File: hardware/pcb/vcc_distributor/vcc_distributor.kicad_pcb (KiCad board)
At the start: 2 copper layers, 40 x 25.5 mm, 12 parts, among them J1 Screw_Terminal_01x02, J2 Conn_01x02, J3 Conn_01x02, J4 Conn_01x02, J5 Conn_01x02, J6 Conn_01x02, J7 Conn_01x02, J8 Conn_01x02

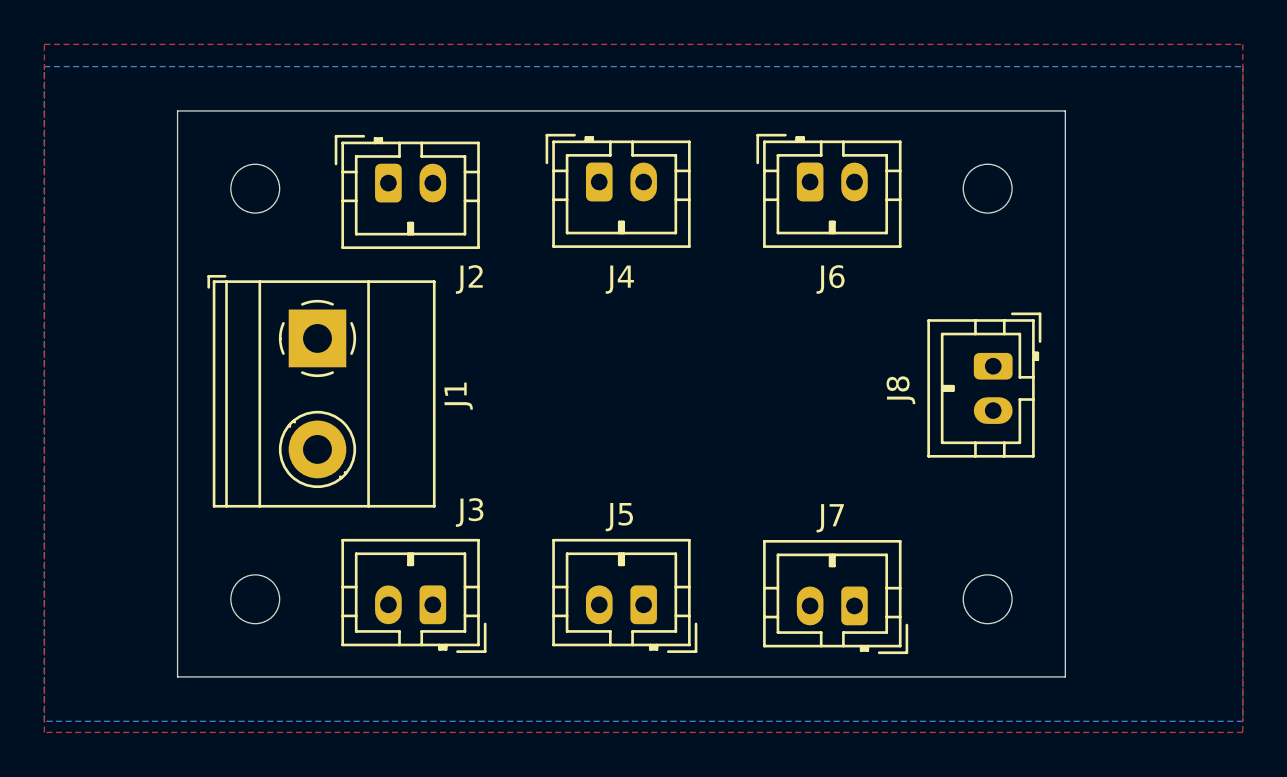
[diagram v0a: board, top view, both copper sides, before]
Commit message: REWORK pcb layout, ADD BOM
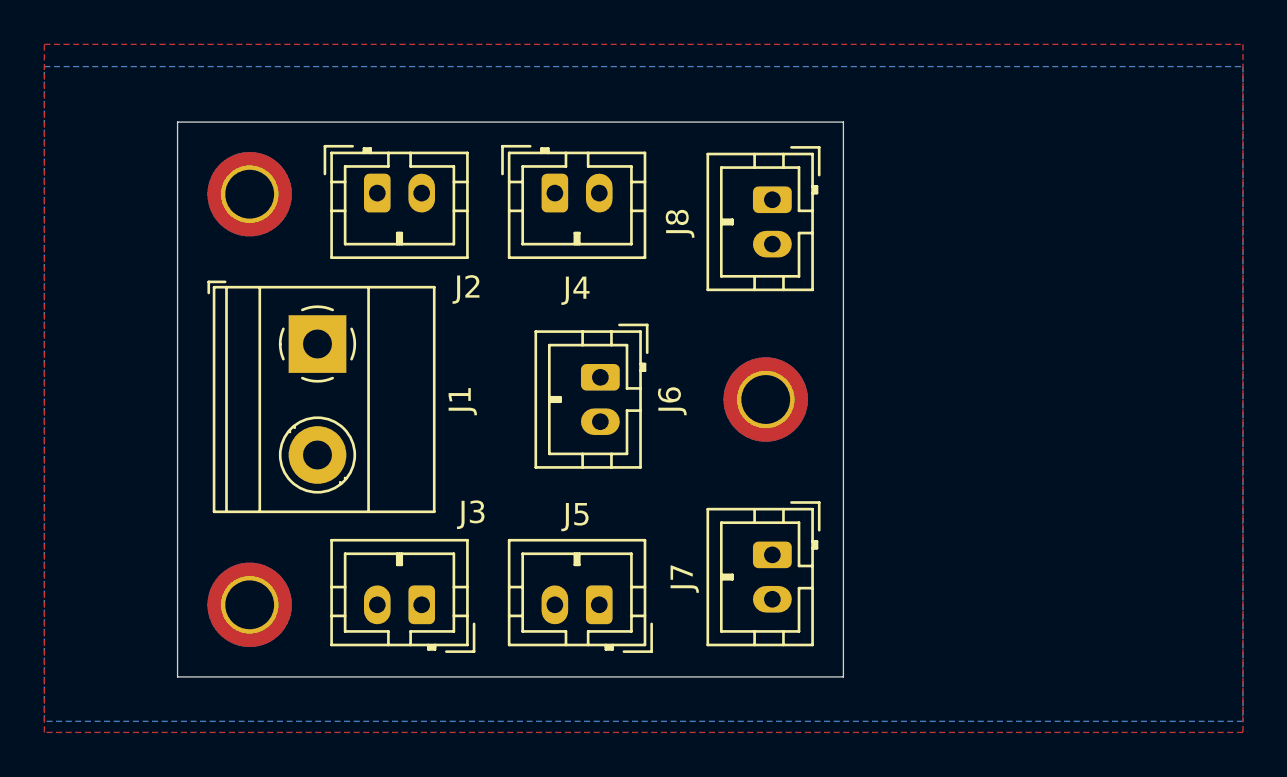
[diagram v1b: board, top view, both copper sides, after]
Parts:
- removed the REF** at (135.5, 49.5)
- REF** (x3): value MountingHole_2.2mm_M2 -> MountingHole_2.2mm_M2_DIN965_Pad_TopBottom; footprint MountingHole:MountingHole_2.2mm_M2 -> MountingHole:MountingHole_2.2mm_M2_DIN965_Pad_TopBottom
- moved REF** 13.5 mm to (125.5, 59.0)
- moved J6 12.9 mm to (118.0, 58.0), turned to -90 degrees
- moved J8 12.5 mm to (125.8, 50.0)
- moved J7 4.36 mm to (125.8, 66.0), turned to -90 degrees
- moved J4 2.06 mm to (116.0, 49.7)
- moved J5 2.00 mm to (118.0, 68.2)
- moved J2 0.67 mm to (108.0, 49.7)
- moved J3 0.50 mm to (110.0, 68.2)
- moved REF** 0.35 mm to (102.2, 68.2)
- moved REF** 0.35 mm to (102.2, 49.8)
- moved J1 0.25 mm to (105.3, 56.5)
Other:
- board size 40 x 25.5 mm -> 30 x 25 mm

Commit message: update gerber files
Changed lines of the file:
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@@
       (outputformat 1)
       (mirror false)
-      (drillshape 1)
+      (drillshape 0)
       (scaleselection 1)
-      (outputdirectory "")
+      (outputdirectory "exports/")
     )
   )
@@
     (fp_line (start -1.95 2.8) (end 3.95 2.8) (layer "F.Fab") (width 0.1))
     (fp_line (start -2.36 -2.11) (end -2.36 -0.86) (layer "F.Fab") (width 0.1))
-    (pad "1" thru_hole roundrect locked (at 0 0 180) (size 1.2 1.75) (drill 0.75) (layers *.Cu *.Mask) (roundrect_rratio 0.208333)
+    (pad "1" thru_hole roundrect locked (at 0 0 180) (size 1.2 1.75) (drill 0.75) (layers *.Cu *.Mask) (roundrect_rratio 0.2083333333)
       (net 1 "GND") (pinfunction "Pin_1") (pintype "passive"))
     (pad "2" thru_hole oval locked (at 2 0 180) (size 1.2 1.75) (drill 0.75) (layers *.Cu *.Mask)
@@
     (fp_line (start -2.36 -2.11) (end -2.36 -0.86) (layer "F.Fab") (width 0.1))
     (fp_line (start -1.11 -2.11) (end -2.36 -2.11) (layer "F.Fab") (width 0.1))
-    (pad "1" thru_hole roundrect locked (at 0 0) (size 1.2 1.75) (drill 0.75) (layers *.Cu *.Mask) (roundrect_rratio 0.208333)
+    (pad "1" thru_hole roundrect locked (at 0 0) (size 1.2 1.75) (drill 0.75) (layers *.Cu *.Mask) (roundrect_rratio 0.2083333333)
       (net 1 "GND") (pinfunction "Pin_1") (pintype "passive"))
     (pad "2" thru_hole oval locked (at 2 0) (size 1.2 1.75) (drill 0.75) (layers *.Cu *.Mask)
@@
     (fp_line (start 3.95 -1.7) (end -1.95 -1.7) (layer "F.Fab") (width 0.1))
     (fp_line (start -1.95 -1.7) (end -1.95 2.8) (layer "F.Fab") (width 0.1))
-    (pad "1" thru_hole roundrect locked (at 0 0 270) (size 1.2 1.75) (drill 0.75) (layers *.Cu *.Mask) (roundrect_rratio 0.208333)
+    (pad "1" thru_hole roundrect locked (at 0 0 270) (size 1.2 1.75) (drill 0.75) (layers *.Cu *.Mask) (roundrect_rratio 0.2083333333)
       (net 1 "GND") (pinfunction "Pin_1") (pintype "passive"))
     (pad "2" thru_hole oval locked (at 2 0 270) (size 1.2 1.75) (drill 0.75) (layers *.Cu *.Mask)
@@
     (fp_line (start -1.95 -1.7) (end -1.95 2.8) (layer "F.Fab") (width 0.1))
     (fp_line (start -1.95 2.8) (end 3.95 2.8) (layer "F.Fab") (width 0.1))
-    (pad "1" thru_hole roundrect locked (at 0 0) (size 1.2 1.75) (drill 0.75) (layers *.Cu *.Mask) (roundrect_rratio 0.208333)
+    (pad "1" thru_hole roundrect locked (at 0 0) (size 1.2 1.75) (drill 0.75) (layers *.Cu *.Mask) (roundrect_rratio 0.2083333333)
       (net 1 "GND") (pinfunction "Pin_1") (pintype "passive"))
     (pad "2" thru_hole oval locked (at 2 0) (size 1.2 1.75) (drill 0.75) (layers *.Cu *.Mask)
@@
     (fp_line (start -1.95 -1.7) (end -1.95 2.8) (layer "F.Fab") (width 0.1))
     (fp_line (start -2.36 -2.11) (end -2.36 -0.86) (layer "F.Fab") (width 0.1))
-    (pad "1" thru_hole roundrect locked (at 0 0 270) (size 1.2 1.75) (drill 0.75) (layers *.Cu *.Mask) (roundrect_rratio 0.208333)
+    (pad "1" thru_hole roundrect locked (at 0 0 270) (size 1.2 1.75) (drill 0.75) (layers *.Cu *.Mask) (roundrect_rratio 0.2083333333)
       (net 1 "GND") (pinfunction "Pin_1") (pintype "passive"))
     (pad "2" thru_hole oval locked (at 2 0 270) (size 1.2 1.75) (drill 0.75) (layers *.Cu *.Mask)
@@
     (fp_line (start -2.36 -2.11) (end -2.36 -0.86) (layer "F.Fab") (width 0.1))
     (fp_line (start -1.95 2.8) (end 3.95 2.8) (layer "F.Fab") (width 0.1))
-    (pad "1" thru_hole roundrect locked (at 0 0 270) (size 1.2 1.75) (drill 0.75) (layers *.Cu *.Mask) (roundrect_rratio 0.208333)
+    (pad "1" thru_hole roundrect locked (at 0 0 270) (size 1.2 1.75) (drill 0.75) (layers *.Cu *.Mask) (roundrect_rratio 0.2083333333)
       (net 1 "GND") (pinfunction "Pin_1") (pintype "passive"))
     (pad "2" thru_hole oval locked (at 2 0 270) (size 1.2 1.75) (drill 0.75) (layers *.Cu *.Mask)
@@
     (fp_line (start 3.95 -1.7) (end -1.95 -1.7) (layer "F.Fab") (width 0.1))
     (fp_line (start -1.95 2.8) (end 3.95 2.8) (layer "F.Fab") (width 0.1))
-    (pad "1" thru_hole roundrect locked (at 0 0 180) (size 1.2 1.75) (drill 0.75) (layers *.Cu *.Mask) (roundrect_rratio 0.208333)
+    (pad "1" thru_hole roundrect locked (at 0 0 180) (size 1.2 1.75) (drill 0.75) (layers *.Cu *.Mask) (roundrect_rratio 0.2083333333)
       (net 1 "GND") (pinfunction "Pin_1") (pintype "passive"))
     (pad "2" thru_hole oval locked (at 2 0 180) (size 1.2 1.75) (drill 0.75) (layers *.Cu *.Mask)
